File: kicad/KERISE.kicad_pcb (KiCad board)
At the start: 2 copper layers, 40 x 44 mm, 105 parts, among them J1 Motor_L, J10 ENC_Slave, J11 ENC_Host, J12 ENC_Slave, J13 Host, J14 Slave, J15 Host, J16 Slave, J2 Motor_R, J3 Host, J4 Slave, J5 Host, J6 Slave, J7 COM, J8 Fan, J9 ENC_Host, P1 ToF_Host, P2 ToF_Slave, Q1 MTM231232LBF, Q10 SFH3015FA, Q11 MTM231232LBF, Q12 DMN3065LW-7, Q13 SFH3015FA, Q14 DMN3065LW-7, Q2 DMN3065LW-7, Q3 SFH3015FA, Q4 MTM231232LBF, Q5 DMN3065LW-7, Q6 SFH3015FA, Q7 DMN3065LW-7, Q8 MTM231232LBF, Q9 DMN3065LW-7, SW1 RESET, SW2 UPLOAD, U1 ESP32-PICO-D4, U2 DRV8835, U3 LXDC2UR30, U4 AS5048A, U5 AS5048A, U6 ICM-20602, U7 ICM-20602, U8 PCA9632, U9 VL6180X

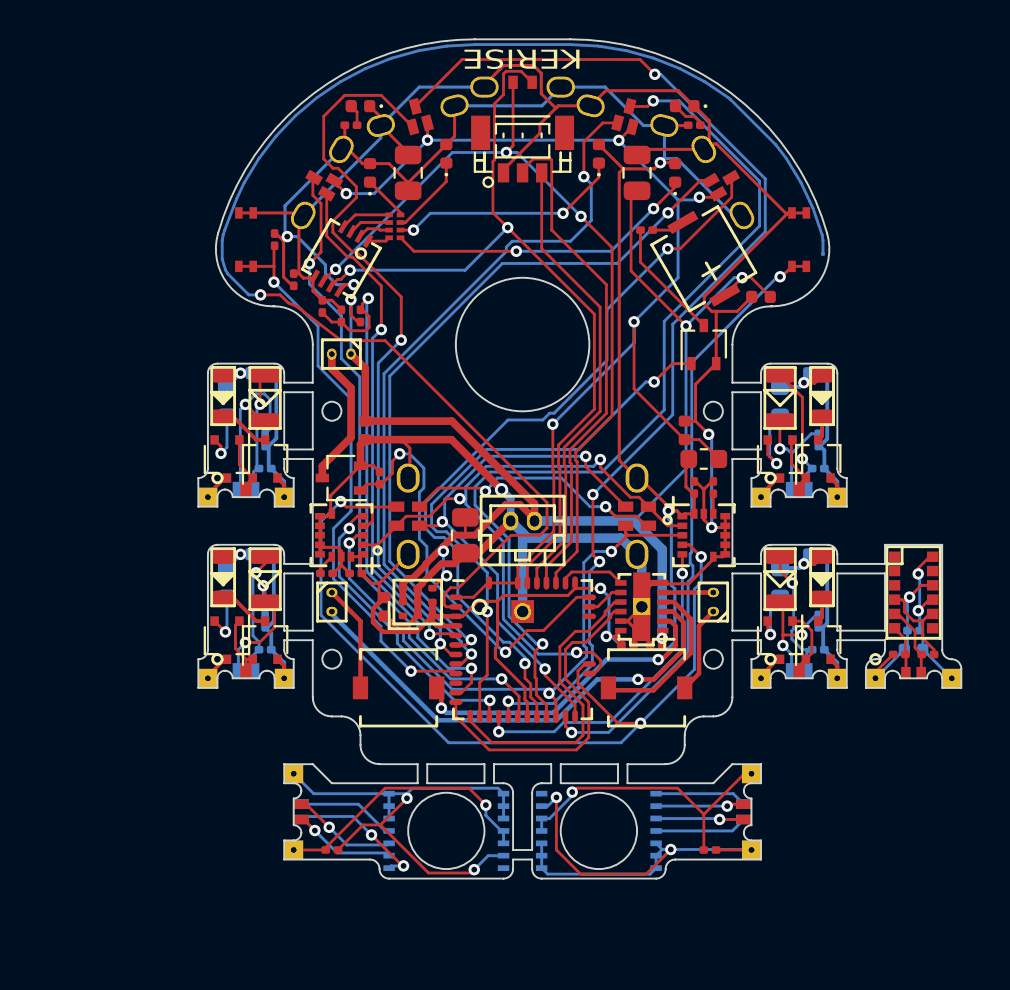
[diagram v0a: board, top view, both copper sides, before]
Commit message: 部品を配置
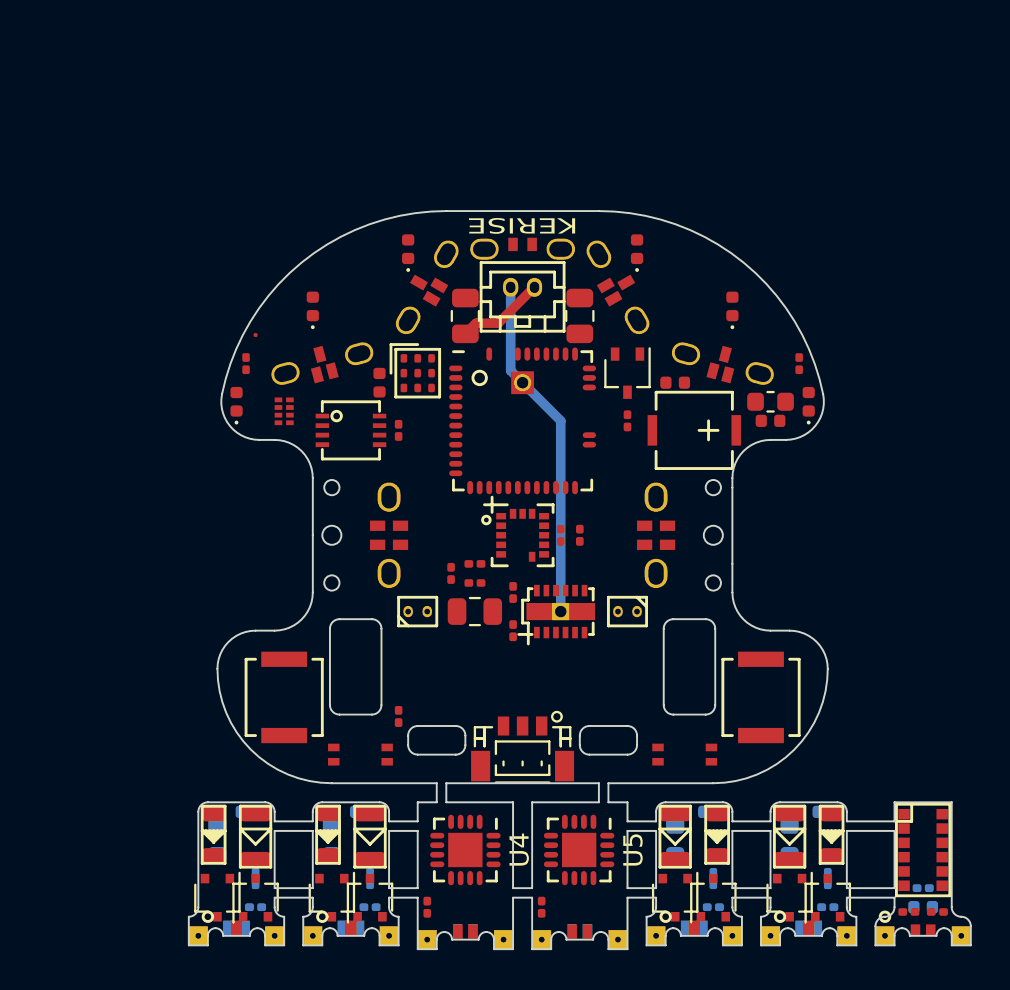
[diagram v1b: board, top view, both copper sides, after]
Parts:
- removed the C13 at (140.2, 107.5)
- removed the C19 at (164.0, 117.5)
- removed the C21 at (164.0, 108.0)
- removed C25: 10u, Capacitor_SMD:C_0402_1005Metric
- removed C26: 4.7u, Capacitor_SMD:C_0402_1005Metric
- removed C27: 0.1u, Capacitor_SMD:C_0201_0603Metric
- removed G***: LOGO, mouse:KERI_9mm
- removed the J10 at (136.5, 127.5)
- removed J16: Slave, mouse:STAND_SLAVE_05
- removed the J8 at (139.0, 103.5)
- removed Q14: DMN3065LW-7, Package_TO_SOT_SMD:SOT-323_SC-70
- removed the R14 at (164.0, 109.5)
- removed R17: 4.7k, Resistor_SMD:R_0201_0603Metric
- removed the U7 at (139.0, 113.0)
- removed U9: VL6180X, mouse:VL6180X
- added C15: 1u, Capacitor_SMD:C_0402_1005Metric, B.Cu at (164.5, 127.5)
- added C22: 10u, Capacitor_SMD:C_0402_1005Metric, F.Cu at (156.5, 105.0)
- added C24: 0.1u, Capacitor_SMD:C_0201_0603Metric, B.Cu at (169.5, 131.5)
- added J13: Slave, mouse:STAND_SLAVE_05, F.Cu at (163.5, 134.0)
- added J9: ENC_Slave, mouse:STAND_SLAVE_06, F.Cu at (145.5, 134.2)
- added R15: 4.7k, Resistor_SMD:R_0201_0603Metric, F.Cu at (168.8, 132.8)
- added U8: VL6180X, mouse:VL6180X, F.Cu at (169.5, 129.5)
- AE1: moved to F.Cu
- C16: moved to B.Cu
- C17: value 0.1u -> 1u; footprint Capacitor_SMD:C_0201_0603Metric -> Capacitor_SMD:C_0402_1005Metric; moved to B.Cu
- C18: value 1u -> 0.1u; footprint Capacitor_SMD:C_0402_1005Metric -> Capacitor_SMD:C_0201_0603Metric
- C20: value 1u -> 0.1u; footprint Capacitor_SMD:C_0402_1005Metric -> Capacitor_SMD:C_0201_0603Metric; moved to F.Cu
- C23: value 0.1u -> 4.7u; footprint Capacitor_SMD:C_0201_0603Metric -> Capacitor_SMD:C_0402_1005Metric; moved to B.Cu
- J11: renamed from J12; moved to F.Cu
- J14: value Slave -> Host; footprint mouse:STAND_SLAVE_05 -> mouse:STAND_HOST_05
- J15: value Host -> Slave; footprint mouse:STAND_HOST_05 -> mouse:STAND_SLAVE_05
- Q10: value SFH3015FA -> MTM231232LBF; footprint mouse:SFH3015FA -> mouse:SOT-323_SC-70
- Q11, Q8: value MTM231232LBF -> DMN3065LW-7
- Q12, Q9: value DMN3065LW-7 -> SFH3015FA; footprint mouse:SOT-323_SC-70 -> mouse:SFH3015FA
- Q13: value SFH3015FA -> DMN3065LW-7; footprint mouse:SFH3015FA -> Package_TO_SOT_SMD:SOT-323_SC-70
- Q7: value DMN3065LW-7 -> MTM231232LBF; footprint Package_TO_SOT_SMD:SOT-323_SC-70 -> mouse:SOT-323_SC-70
- R10: value 10k -> 100; footprint Resistor_SMD:R_0201_0603Metric -> Resistor_SMD:R_0603_1608Metric; moved to B.Cu
- R11, R13: value 100 -> 10k; footprint Resistor_SMD:R_0603_1608Metric -> Resistor_SMD:R_0201_0603Metric
- R12: value 10k -> 100; footprint Resistor_SMD:R_0201_0603Metric -> Resistor_SMD:R_0603_1608Metric
- U4, U5: value AS5048A -> MA730; footprint mouse:TSSOP-14_4.4x5mm_Pitch0.65mm -> Package_DFN_QFN:QFN-16-1EP_3x3mm_P0.5mm_EP1.8x1.8mm; moved to F.Cu
- moved J15 43.1 mm to (157.5, 134.0), turned to 0 degrees
- moved C23 35.8 mm to (169.5, 132.5)
- moved Q7 32.2 mm to (162.5, 132.0), turned to 270 degrees
- moved J7 31.0 mm to (148.5, 124.0), turned to 180 degrees
- moved AE1 30.1 mm to (134.5, 102.5)
- moved C16 29.5 mm to (164.5, 131.0), turned to 270 degrees
- moved R10 28.7 mm to (162.5, 129.0)
- moved SW1 27.7 mm to (140.0, 124.5), turned to 180 degrees
- moved SW2 27.7 mm to (157.0, 124.5), turned to 180 degrees
- moved R13 26.7 mm to (158.5, 132.5), turned to 0 degrees
- moved R1 25.8 mm to (142.0, 122.5)
- moved C2 24.5 mm to (146.0, 117.0), turned to 0 degrees
- moved Q3 23.6 mm to (140.5, 128.8)
- moved C10 23.6 mm to (140.5, 131.0)
- moved C9 23.6 mm to (140.2, 127.5)
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- renumbered C14 to C13, C15 to C14, C22 to C19, C24 to C21, J11 to J10, J13 to J12, J9 to J8, R15 to R14, U8 to U7
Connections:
- C16 pad 1: +3V3 -> /IR_RCV_FL/s_AVDD
- C16 pad 2: GND -> /IR_RCV_FL/s_GND
- C17 pad 1: Net-(C17-Pad1) -> /IR_RCV_FR/LED_to_C
- C17 pad 2: GND -> /IR_RCV_FR/s_GND
- C18 pad 1: /IR_RCV_FL/LED_to_C -> /IR_RCV_FR/s_AVDD
- C18 pad 2: /IR_RCV_FL/s_GND -> /IR_RCV_FR/s_GND
- C20 pad 1: /IR_RCV_FR/LED_to_C -> Net-(C20-Pad1)
- C20 pad 2: /IR_RCV_FR/s_GND -> GND
- C23 pad 1: Net-(C23-Pad1) -> /ToF/s_3.3V
- C23 pad 2: GND -> /ToF/s_GND
- J10 pad 2: SPI-CS-ENC -> SPI-CS-ENC_L
- J10 pad 4: ENC-CHAIN -> SPI-MOSI
- J14 pad 1: /IR_RCV_FL/s_3.3V -> +3V3
- J14 pad 2: /IR_RCV_FL/s_AVDD -> VDDA
- J14 pad 3: /IR_RCV_FL/s_IR_LED -> PR-LED-FR
- J14 pad 4: /IR_RCV_FL/s_IR_RCV -> PR-RCV-FR
- J14 pad 5: /IR_RCV_FL/s_GND -> GND
- J15 pad 1: +3V3 -> /IR_RCV_FR/s_3.3V
- J15 pad 2: VDDA -> /IR_RCV_FR/s_AVDD
- J15 pad 3: PR-LED-FR -> /IR_RCV_FR/s_IR_LED
- J15 pad 4: PR-RCV-FR -> /IR_RCV_FR/s_IR_RCV
- J15 pad 5: GND -> /IR_RCV_FR/s_GND
- J8 pad 2: SPI-CS-ENC -> SPI-CS-ENC_R
- J8 pad 5: ENC-CHAIN -> SPI-MISO
- Q10 pad 1: /IR_RCV_FL/s_AVDD -> /IR_RCV_FR/s_IR_LED
- Q10 pad 2: /IR_RCV_FL/s_IR_RCV -> Net-(Q10-Pad2)
- Q11 pad 2: Net-(Q11-Pad2) -> /IR_RCV_FR/s_GND
- Q11 pad 3: /IR_RCV_FR/s_3.3V -> /IR_RCV_FR/LED_to_FET
- Q12 pad 1: /IR_RCV_FR/s_IR_LED -> /IR_RCV_FR/s_AVDD
- Q12 pad 2: /IR_RCV_FR/s_GND -> /IR_RCV_FR/s_IR_RCV
- Q13 pad 1: /IR_RCV_FR/s_AVDD -> SPEAKER
- Q13 pad 2: /IR_RCV_FR/s_IR_RCV -> GND
- Q7 pad 1: FAN -> /IR_RCV_FL/s_IR_LED
- Q7 pad 2: GND -> Net-(Q7-Pad2)
- Q7 pad 3: /Fan/fan_to_fet -> /IR_RCV_FL/s_3.3V
- Q8 pad 2: Net-(Q8-Pad2) -> /IR_RCV_FL/s_GND
- Q8 pad 3: /IR_RCV_FL/s_3.3V -> /IR_RCV_FL/LED_to_FET
- Q9 pad 1: /IR_RCV_FL/s_IR_LED -> /IR_RCV_FL/s_AVDD
- Q9 pad 2: /IR_RCV_FL/s_GND -> /IR_RCV_FL/s_IR_RCV
- R10 pad 1: FAN -> Net-(Q7-Pad2)
- R10 pad 2: GND -> /IR_RCV_FL/LED_to_C
- R11 pad 1: Net-(Q8-Pad2) -> /IR_RCV_FL/s_IR_RCV
- R11 pad 2: /IR_RCV_FL/LED_to_C -> /IR_RCV_FL/s_GND
- R12 pad 1: /IR_RCV_FL/s_IR_RCV -> Net-(Q10-Pad2)
- R12 pad 2: /IR_RCV_FL/s_GND -> /IR_RCV_FR/LED_to_C
- R13 pad 1: Net-(Q11-Pad2) -> /IR_RCV_FR/s_IR_RCV
- R13 pad 2: /IR_RCV_FR/LED_to_C -> /IR_RCV_FR/s_GND
- R14 pad 2: Net-(Q14-Pad3) -> Net-(Q13-Pad3)
- R16 pad 2: /ToF/s_SDA -> /ToF/s_SCL
- U1 pad 15: SPI-CS-IMU_L -> SPI-CS-IMU
- U1 pad 16: SPI-CS-IMU_R -> (no net)
- U1 pad 24: SPI-CS-ENC -> SPI-CS-ENC_L
- U1 pad 34: (no net) -> SPI-CS-ENC_R
- U1 pad 36: FAN -> (no net)
- U4 pad 1: /Encoder_R/s_CS -> (no net)
- U4 pad 11: /Encoder_R/s_VDD -> (no net)
- U4 pad 12: /Encoder_R/s_VDD -> /Encoder_R/s_SCLK
- U4 pad 13: /Encoder_R/s_GND -> /Encoder_R/s_VDD
- U4 pad 2: /Encoder_R/s_SCLK -> (no net)
- U4 pad 3: /Encoder_R/s_MISO -> (no net)
- U4 pad 5: /Encoder_R/s_GND -> /Encoder_R/s_CS
- U4 pad 6: /Encoder_R/s_GND -> (no net)
- U4 pad 7: /Encoder_R/s_GND -> /Encoder_R/s_MISO
- U4 pad 9: /Encoder_R/s_GND -> (no net)
- U5 pad 1: /Encoder_L/s_CS -> (no net)
- U5 pad 11: /Encoder_L/s_VDD -> (no net)
- U5 pad 12: /Encoder_L/s_VDD -> /Encoder_L/s_SCLK
- U5 pad 13: /Encoder_L/s_GND -> /Encoder_L/s_VDD
- U5 pad 2: /Encoder_L/s_SCLK -> (no net)
- U5 pad 3: /Encoder_L/s_MISO -> (no net)
- U5 pad 5: /Encoder_L/s_GND -> /Encoder_L/s_CS
- U5 pad 6: /Encoder_L/s_GND -> (no net)
- U5 pad 7: /Encoder_L/s_GND -> /Encoder_L/s_MISO
- U5 pad 9: /Encoder_L/s_GND -> (no net)
- U6 pad 14: Net-(C17-Pad1) -> Net-(C20-Pad1)
- U6 pad 5: SPI-CS-IMU_R -> SPI-CS-IMU
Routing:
- net GND: track 144.1 -> 18.1 mm, vias 3 -> 0
- net +3V3: track 120.5 -> 0.00 mm, vias 6 -> 0
- net /ANTENA: track 74.5 -> 0.00 mm, vias 1 -> 0
- net +BATT: track 73.0 -> 4.58 mm, vias 6 -> 0
- net VDDA: track 61.6 -> 0.00 mm, vias 6 -> 0
- net PR-LED-FL: track 57.7 -> 0.00 mm, vias 4 -> 0
- net PR-LED-FR: track 48.4 -> 0.00 mm, vias 2 -> 0
- net SPI-MISO: track 47.6 -> 0.00 mm, vias 3 -> 0
- net I2C-SDA: track 43.0 -> 0.00 mm, vias 2 -> 0
- net I2C-SCL: track 42.7 -> 0.00 mm, vias 3 -> 0
- net PR-LED-SR: track 39.4 -> 0.00 mm, vias 2 -> 0
- net PR-RCV-FL: track 39.3 -> 0.00 mm, vias 2 -> 0
- net PR-RCV-FR: track 38.4 -> 0.00 mm, vias 2 -> 0
- net PR-RCV-SR: track 37.7 -> 0.00 mm, vias 2 -> 0
- net SPI-SCLK: track 34.9 -> 0.00 mm, vias 3 -> 0
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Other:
- board size 40 x 44 mm -> 41 x 38.7 mm
- board text removed: "2019.01.17"

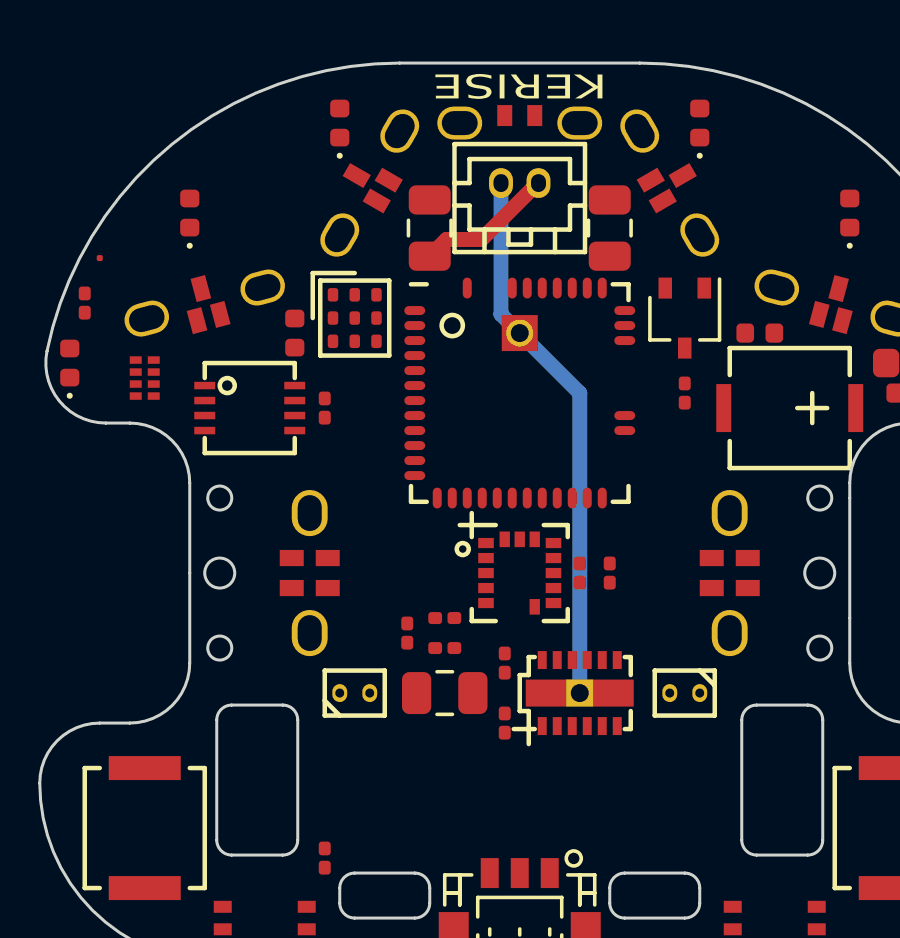
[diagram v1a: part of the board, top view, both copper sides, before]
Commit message: 未配線あり
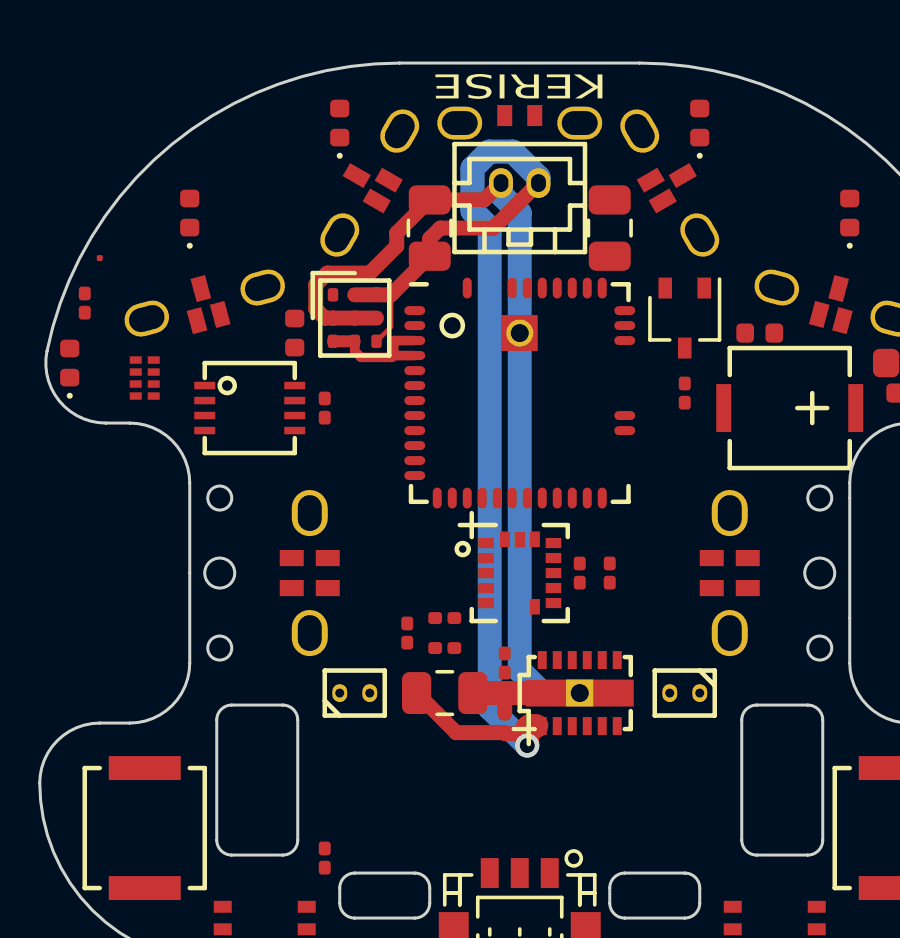
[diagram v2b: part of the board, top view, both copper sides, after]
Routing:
- net +BATT: track 4.58 -> 38.5 mm, vias 0 -> 1
- net GND: track 18.1 -> 36.3 mm
- net +3V3: track 0.00 -> 4.36 mm

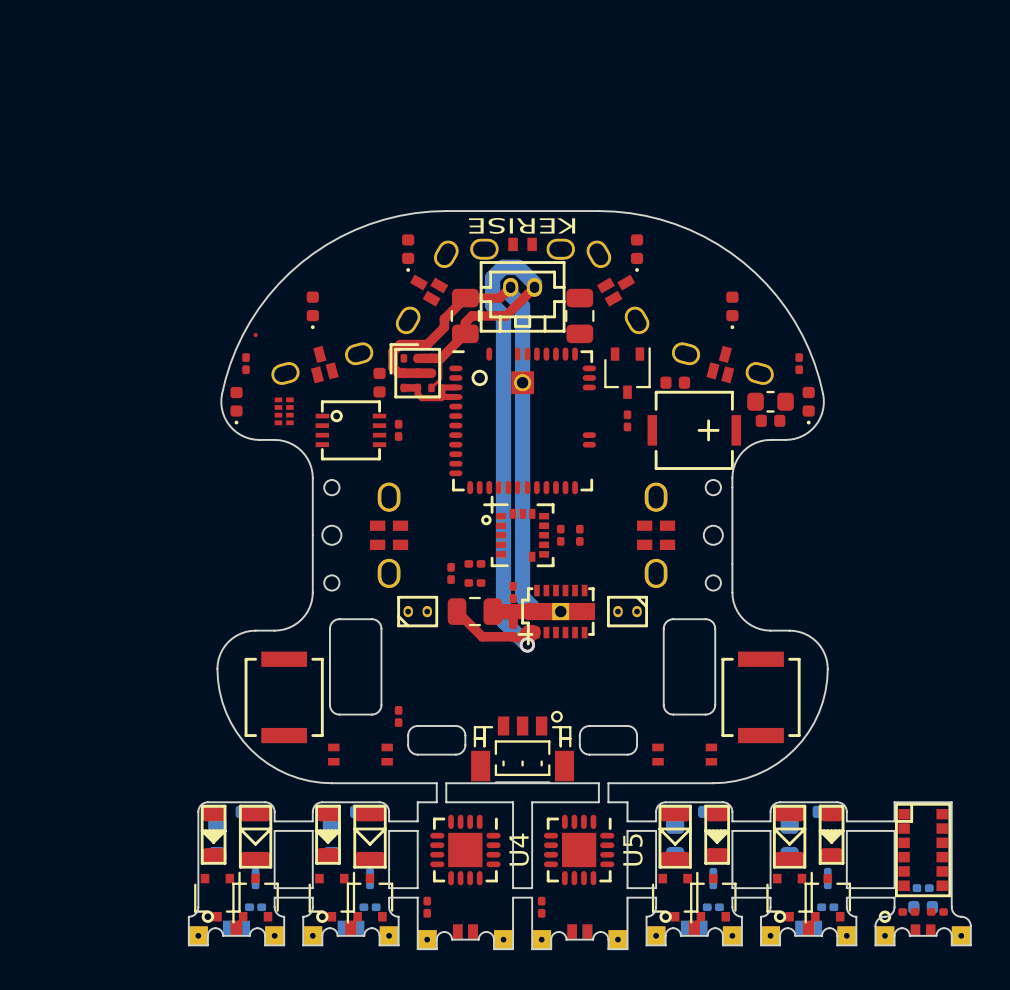
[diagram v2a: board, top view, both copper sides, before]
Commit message: 配線幅を改良
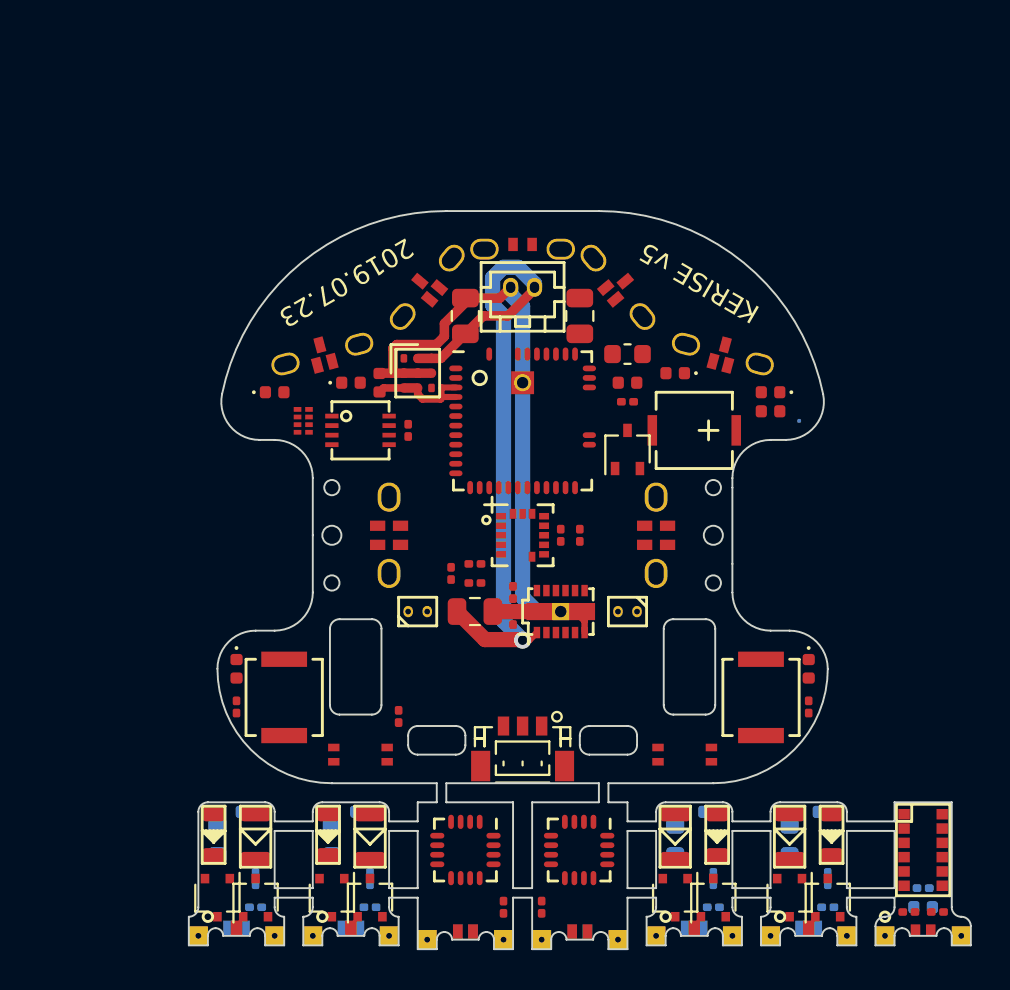
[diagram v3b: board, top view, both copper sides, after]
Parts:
- added G***: LOGO, mouse:KERI_9mm, B.Cu at (148.5, 113.0)
- AE1: moved to B.Cu
- U4, U5: footprint Package_DFN_QFN:QFN-16-1EP_3x3mm_P0.5mm_EP1.8x1.8mm -> mouse:QFN-16-1EP_3x3mm_P0.5mm
- moved AE1 28.9 mm to (163.0, 107.0)
- moved R4 18.0 mm to (133.5, 122.0), turned to 90 degrees
- moved R5 18.0 mm to (163.5, 122.0), turned to 90 degrees
- moved D1 14.0 mm to (133.5, 120.0), turned to 270 degrees
- moved D2 14.0 mm to (163.5, 120.0), turned to 270 degrees
- moved L3 7.91 mm to (154.0, 103.5)
- moved C8 7.76 mm to (154.0, 105.0)
- moved D9 7.62 mm to (139.5, 105.0), turned to 0 degrees
- moved D8 6.80 mm to (156.5, 104.5), turned to 180 degrees
- moved C22 5.22 mm to (161.5, 106.5), turned to 0 degrees
- moved D10 4.92 mm to (135.5, 105.5), turned to 0 degrees
- moved D7 4.92 mm to (161.5, 105.5), turned to 180 degrees
- moved C13 4.00 mm to (147.5, 132.5)
- moved Q13 4.00 mm to (154.0, 108.5), turned to 90 degrees
- moved RN1 1.12 mm to (137.0, 107.0)
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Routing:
- net +BATT: track 38.5 -> 35.3 mm
- net +3V3: track 4.36 -> 7.22 mm
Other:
- net class Motor: trace_width 0.24 -> 0.34
- board text added: "2019.07.23"
- board text added: "KERISE v5"
- board text removed: "KERISE"

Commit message: エンコーダー基板の位置を調整
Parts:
- removed G***: LOGO, mouse:KERI_9mm
- moved R1 13.5 mm to (142.5, 109.0), turned to 270 degrees
- moved C21 2.50 mm to (141.0, 105.5), turned to 0 degrees
- moved C1 2.36 mm to (143.0, 106.2), turned to 0 degrees
- moved D9 1.12 mm to (140.5, 104.5)
- moved D10 1.00 mm to (136.5, 105.5)
- moved D7 1.00 mm to (160.5, 105.5)
- moved C22 0.50 mm to (161.5, 107.0)
- moved J10 0.50 mm to (141.0, 113.0)
- moved J8 0.50 mm to (156.0, 113.0)
- turned C10 to 0 degrees
- turned C12 to 0 degrees
- turned C16 to 0 degrees
- turned C18 to 0 degrees
- turned J1 to 180 degrees
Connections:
- L1 pad 1: /Motor/MT_OUT_L1 -> /Motor/MT_OUT_L2
- U2 pad 2: /Motor/MT_OUT_L_L -> /Motor/MT_OUT_L1
- U2 pad 3: /Motor/MT_OUT_L2 -> /Motor/MT_OUT_L_L
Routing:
- net GND: track 36.5 -> 40.0 mm
